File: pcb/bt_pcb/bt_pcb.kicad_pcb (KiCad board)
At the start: 4 copper layers, 130 x 65 mm, 224 parts, among them IC1 LTC3621EMS8E-25#PBF, IC2 ADAU1961WBCPZ-R7, IC3 STM32H750VBT6, IC4 STM32H523CEU6, IC5 W25Q512JVEIM, J1 Conn_01x02, J10 Conn_01x04, J11 Conn_01x04, J12 Conn_01x05, J13 FTSH-107-01-L-DV-K-A, J14 FTSH-107-01-L-DV-K-A, J15 Conn_01x08, J16 ReanNYS216G, J17 ReanNYS216G, J18 ReanNYS216G, J19 ReanNYS216G, J2 694106301002, J3 Conn_01x01, J4 Conn_01x01, J5 Conn_01x03, J6 UJ32-C-H-G-SMT-TR-68, J7 Conn_01x04, J8 Conn_01x10, J9 Conn_01x04, SW1 SW_Push, SW2 SW_Push, SW3 SW_Push, SW4 SW_Push, SW5 SW_Push, SW6 SW_Push, SW7 SW_Push, SW8 SW_Push, SW9 SW_Push, U1 TLV76133DCY, U2 TLV76133DCY, U3 MCP6004, U4 MCP6004

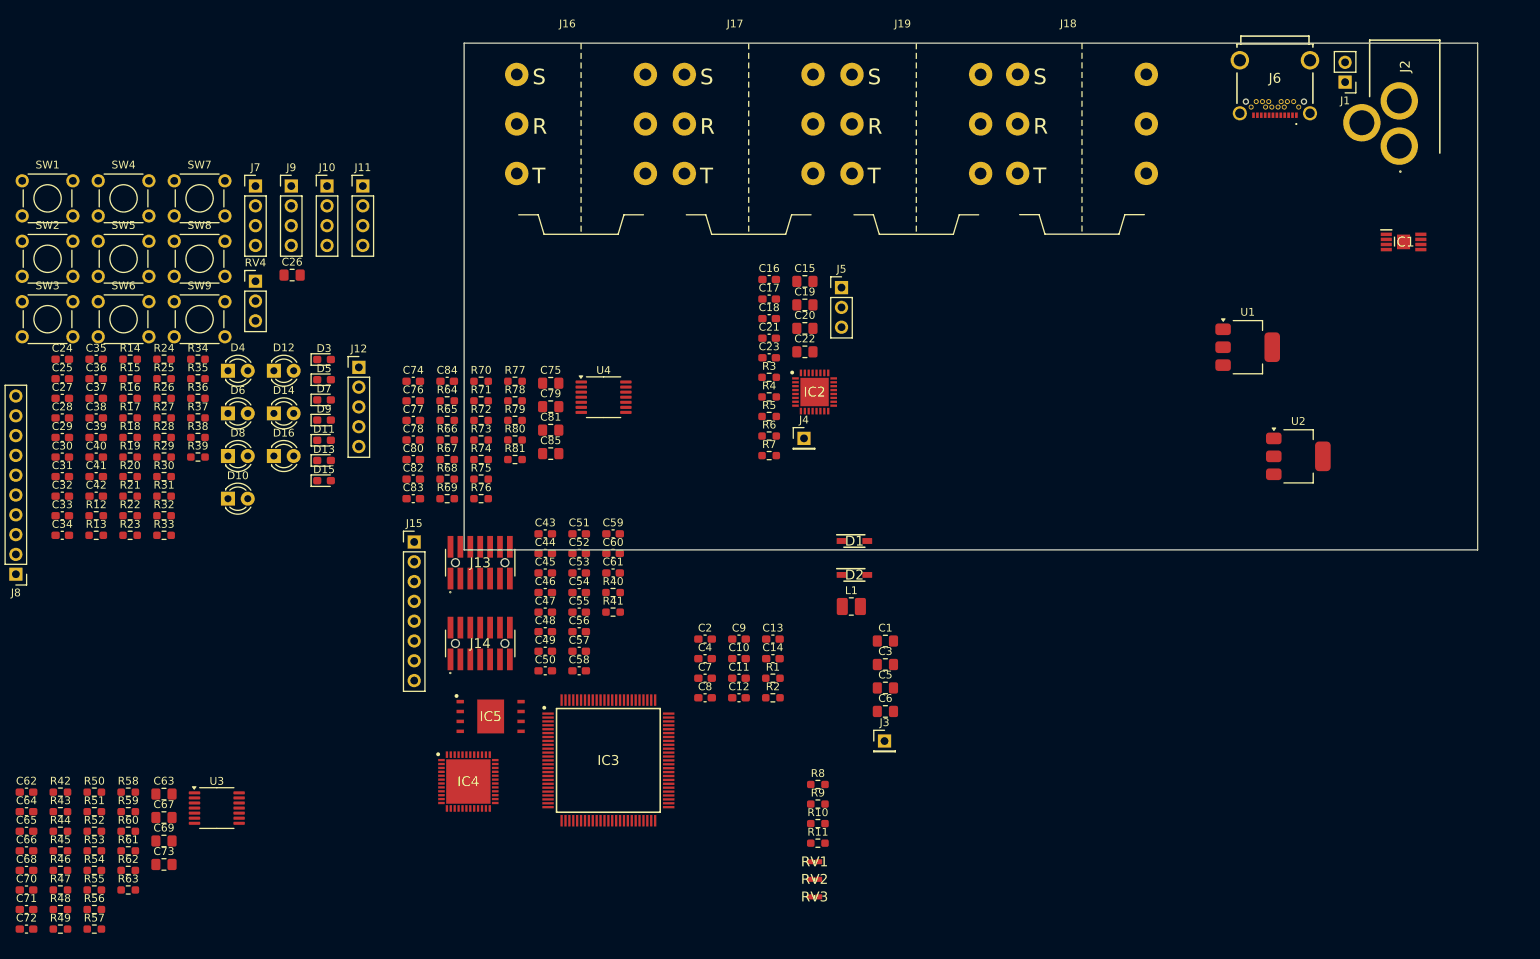
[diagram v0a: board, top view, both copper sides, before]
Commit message: pcb with some schematic tuning
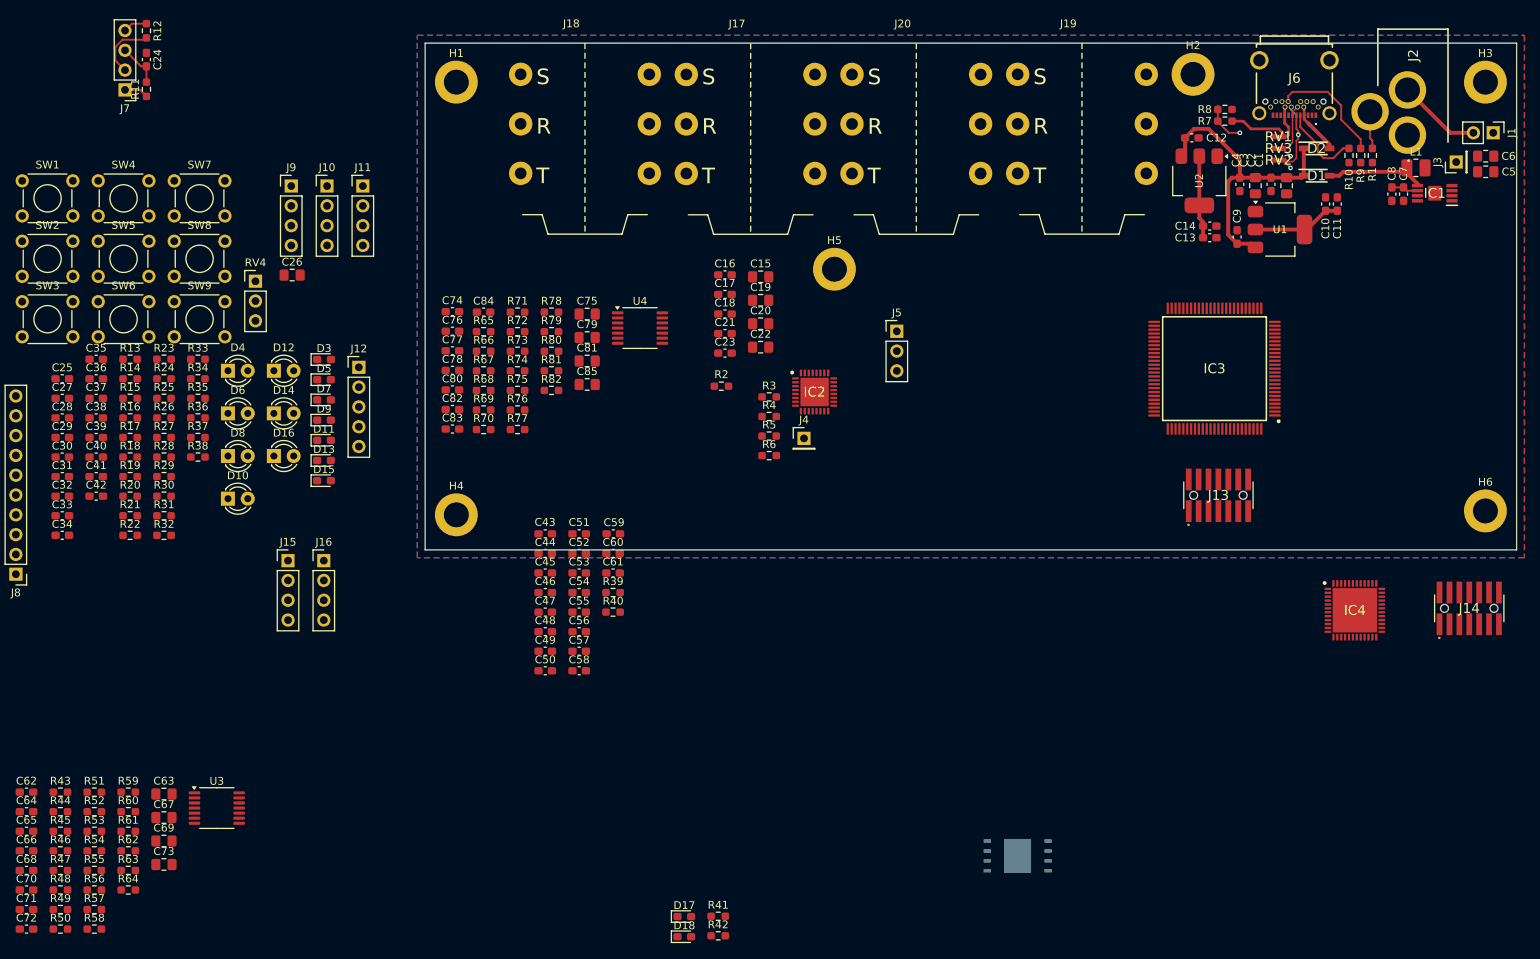
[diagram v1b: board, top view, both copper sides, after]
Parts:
- removed the R2 at (124.6, 151.5)
- added D17: LED, LED_SMD:LED_0603_1608Metric_Pad1.05x0.95mm_HandSolder, F.Cu at (113.2, 179.5)
- added D18: LED, LED_SMD:LED_0603_1608Metric_Pad1.05x0.95mm_HandSolder, F.Cu at (113.2, 182.1)
- added H1: MountingHole_Pad, MountingHole:MountingHole_3.2mm_M3_ISO14580_Pad, F.Cu at (84.0, 72.5)
- added H2: MountingHole_Pad, MountingHole:MountingHole_3.2mm_M3_ISO14580_Pad, F.Cu at (178.5, 71.5)
- added H3: MountingHole_Pad, MountingHole:MountingHole_3.2mm_M3_ISO14580_Pad, F.Cu at (216.0, 72.5)
- added H4: MountingHole_Pad, MountingHole:MountingHole_3.2mm_M3_ISO14580_Pad, F.Cu at (84.0, 128.0)
- added H5: MountingHole_Pad, MountingHole:MountingHole_3.2mm_M3_ISO14580_Pad, F.Cu at (132.5, 96.5)
- added H6: MountingHole_Pad, MountingHole:MountingHole_3.2mm_M3_ISO14580_Pad, F.Cu at (216.0, 127.5)
- added J16: Conn_01x04, Connector_PinHeader_2.54mm:PinHeader_1x04_P2.54mm_Vertical, F.Cu at (67.0, 133.9)
- added R41: 680, Resistor_SMD:R_0603_1608Metric_Pad0.98x0.95mm_HandSolder, F.Cu at (117.6, 179.5)
- added R42: 680, Resistor_SMD:R_0603_1608Metric_Pad0.98x0.95mm_HandSolder, F.Cu at (117.6, 182.0)
- IC5: moved to B.Cu
- J15: value Conn_01x08 -> Conn_01x04; footprint Connector_PinHeader_2.54mm:PinHeader_1x08_P2.54mm_Vertical -> Connector_PinHeader_2.54mm:PinHeader_1x04_P2.54mm_Vertical
- moved J14 126.9 mm to (213.9, 140.0)
- moved IC4 115.8 mm to (199.2, 140.2)
- moved RV3 112.9 mm to (189.4, 81.0)
- moved R10 111.5 mm to (198.5, 81.9), turned to -90 degrees
- moved R9 110.4 mm to (200.0, 81.9), turned to -90 degrees
- moved RV1 110.4 mm to (189.4, 79.5)
- moved RV2 109.8 mm to (189.4, 82.5)
- moved C8 109.2 mm to (204.0, 86.9), turned to -90 degrees
- moved C7 109.0 mm to (205.5, 86.9), turned to -90 degrees
- moved C6 104.9 mm to (216.0, 82.0)
- moved J3 104.4 mm to (212.2, 82.8), turned to 90 degrees
- moved R8 103.3 mm to (182.6, 76.0)
- moved R1 102.0 mm to (201.5, 81.9), turned to -90 degrees
- moved C5 101.6 mm to (216.0, 84.0)
- moved R7 99.8 mm to (182.6, 77.5), turned to 180 degrees
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- renumbered J16 to J17, J17 to J18, J18 to J19, J19 to J20, R11 to R10, R12 to R11, R13 to R12, R14 to R13, R15 to R14, R16 to R15, R17 to R16, R18 to R17, R19 to R18, R20 to R19, R3 to R2, R21 to R20, R22 to R21, R23 to R22, R24 to R23, R25 to R24, R26 to R25, R27 to R26, R28 to R27, R29 to R28, R30 to R29, R4 to R3, R31 to R30, R32 to R31, R33 to R32, R34 to R33, R35 to R34, R36 to R35, R37 to R36, R38 to R37, R39 to R38, R40 to R39, R5 to R4, R41 to R40, R42 to R43, R43 to R44, R44 to R45, R45 to R46, R46 to R47, R47 to R48, R48 to R49, R6 to R5, R49 to R50, R50 to R51, R51 to R52, R52 to R53, R53 to R54, R54 to R55, R55 to R56, R56 to R57, R57 to R58, R58 to R59, R7 to R6, R59 to R60, R60 to R61, R61 to R62, R62 to R63, R63 to R64, R64 to R65, R65 to R66, R66 to R67, R67 to R68, R68 to R69, R8 to R7, R69 to R70, R70 to R71, R71 to R72, R72 to R73, R73 to R74, R74 to R75, R75 to R76, R76 to R77, R77 to R78, R78 to R79, R9 to R8, R79 to R80, R80 to R81, R81 to R82, R10 to R9
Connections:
- C1 pad 1: Net-(D1-A) -> +5V
- C2 pad 1: Net-(D1-A) -> +5V
- C3 pad 1: Net-(D1-A) -> +5V
- C4 pad 1: Net-(D1-A) -> +5V
- C5 pad 1: Net-(IC1-VIN) -> Net-(IC1-RUN)
- C6 pad 1: Net-(IC1-VIN) -> Net-(IC1-RUN)
- IC1 pad 2: Net-(IC1-VIN) -> Net-(IC1-RUN)
- IC3 pad 65: GND -> AUX_1_TO_2
- IC3 pad 66: GND -> AUX_2_TO_1
- IC4 pad 10: GND -> AUX_2_TO_1
- IC4 pad 11: GND -> AUX_1_TO_2
- J1 pad 2: Net-(IC1-VIN) -> Net-(IC1-RUN)
- J15 pad 1: Net-(IC4-PB10) -> Net-(IC4-PA7)
- J15 pad 2: Net-(IC4-PB2) -> Net-(IC4-PA6)
- J15 pad 3: Net-(IC4-PB1) -> Net-(IC4-PA5)
- J15 pad 4: Net-(IC4-PB0) -> Net-(IC4-PA4)
- J2 pad 2: Net-(IC1-VIN) -> Net-(IC1-RUN)
- J6 pad A10: unconnected-(J6-SSRXN2-PadA10) -> GND
- J6 pad A11: unconnected-(J6-SSRXP2-PadA11) -> GND
- J6 pad A2: unconnected-(J6-SSTXP1-PadA2) -> GND
- J6 pad A3: unconnected-(J6-SSTXN1-PadA3) -> GND
- J6 pad A8: unconnected-(J6-SBU1-PadA8) -> GND
- J6 pad B10: unconnected-(J6-SSRXN1-PadB10) -> GND
- J6 pad B11: unconnected-(J6-SSRXP1-PadB11) -> GND
- J6 pad B2: unconnected-(J6-SSTXP2-PadB2) -> GND
- J6 pad B3: unconnected-(J6-SSTXN2-PadB3) -> GND
- J6 pad B8: unconnected-(J6-SBU2-PadB8) -> GND
- L1 pad 1: Net-(IC1-SW) -> Net-(D1-A)
- L1 pad 2: Net-(D1-A) -> Net-(IC1-SW)
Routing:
- net +5V: track 0.00 -> 38.6 mm
- net VBUS: track 0.00 -> 22.7 mm
- net Net-(J6-CC2): track 0.00 -> 15.0 mm
- net +3V3: track 0.00 -> 14.6 mm
- net USB_D-: track 0.00 -> 13.2 mm, vias 0 -> 2
- net Net-(D1-A): track 0.00 -> 12.3 mm
- net Net-(IC1-RUN): track 0.00 -> 10.7 mm
- net +3.3VA: track 0.00 -> 10.7 mm
- net Net-(J6-CC1): track 0.00 -> 10.5 mm
- net EXP_SW_0: track 0.00 -> 7.96 mm
- net USB_D+: track 0.00 -> 7.87 mm, vias 0 -> 1
- net EXP_0: track 0.00 -> 5.63 mm
- net VBUS_SENSE: track 0.00 -> 5.50 mm, vias 0 -> 1
- net Net-(J2-GND_2): track 0.00 -> 4.82 mm
- net Net-(IC1-INTVCC): track 0.00 -> 3.61 mm
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- added copper zone on B.Cu, net GND
- added copper zone on F.Cu, net GND
- added copper zone on In1.Cu, net GND
- added copper zone on In2.Cu, net GND
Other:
- board size 130 x 65 mm -> 140 x 65 mm

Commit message: idk
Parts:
- moved SW6 179.7 mm to (217.8, 100.2), turned to 180 degrees
- moved C39 176.8 mm to (212.9, 93.5)
- moved C40 175.9 mm to (212.9, 103.5)
- moved C41 175.3 mm to (212.8, 113.5)
- moved C42 175.1 mm to (212.9, 123.5)
- moved SW9 172.5 mm to (217.8, 130.2), turned to 180 degrees
- moved SW8 172.1 mm to (217.8, 120.2), turned to 180 degrees
- moved SW7 171.8 mm to (217.8, 110.2), turned to 180 degrees
- moved R35 166.5 mm to (216.2, 93.5)
- moved R36 165.7 mm to (216.2, 103.5)
- moved R38 165.4 mm to (216.2, 123.5)
- moved R37 165.4 mm to (216.1, 113.5)
- moved R26 162.3 mm to (208.2, 101.0)
- moved R27 161.9 mm to (208.2, 111.0)
- moved R29 161.9 mm to (208.2, 131.0)
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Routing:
- net +3V3: track 14.6 -> 65.0 mm
- net EXP_SW_0: track 7.96 -> 3.25 mm
- net Net-(IC1-RUN): track 10.7 -> 15.4 mm
- net EXP_2: track 0.00 -> 4.28 mm
- net EXP_1: track 0.00 -> 4.28 mm
- net EXP_3: track 0.00 -> 4.28 mm
- net GND: track 3.09 -> 0.00 mm
- net EXP_SW_3: track 0.00 -> 3.00 mm
- net EXP_SW_2: track 0.00 -> 3.00 mm
- net EXP_SW_1: track 0.00 -> 3.00 mm
- net Net-(D1-A): track 12.3 -> 9.96 mm
- net Net-(IC1-INTVCC): track 3.61 -> 1.64 mm
- net VBUS: track 22.7 -> 20.9 mm
- net USB_D+: track 7.87 -> 6.16 mm
- net +5V: track 38.6 -> 37.2 mm
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
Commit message: progress
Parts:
- C74, C75, C76, C77, C78, C79, C80, C81, C82, C83, C84, C85, R65, R66, R67, R68, R69, R70, R71, R72, R73, R74, R75, R76, U4: moved to B.Cu
- moved J14 272.2 mm to (-55.8, 103.8)
- moved IC4 221.5 mm to (-57.4, 121.5), turned to 0 degrees
- moved J13 216.1 mm to (-55.8, 93.4)
- moved IC5 176.1 mm to (-9.75, 93.8), turned to 0 degrees
- moved R41 174.4 mm to (-38.8, 102.3)
- moved R42 174.4 mm to (-38.8, 104.8)
- moved D17 166.8 mm to (-34.4, 102.0)
- moved D18 166.8 mm to (-34.4, 104.5)
- moved J5 161.8 mm to (-19.1, 131.3)
- moved J4 155.9 mm to (-23.9, 150.7)
- moved R3 155.9 mm to (-28.4, 145.3)
- moved R4 155.9 mm to (-28.4, 147.9)
- moved R5 155.9 mm to (-28.4, 150.4)
- moved R6 155.9 mm to (-28.4, 152.9)
- moved IC2 155.9 mm to (-22.5, 144.7)
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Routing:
- net +3V3: track 65.0 -> 105.0 mm
- net +5V: track 37.2 -> 0.00 mm
- net EXP_SW_0: track 3.25 -> 22.3 mm
- net EXP_0: track 4.38 -> 20.9 mm
- net Net-(IC1-RUN): track 15.4 -> 31.2 mm
- net EXP_SW_1: track 3.00 -> 16.4 mm
- net EXP_1: track 4.28 -> 15.9 mm
- net BTN_7_QB: track 0.00 -> 10.9 mm
- net BTN_6_QB: track 0.00 -> 10.9 mm
- net BTN_5_QB: track 0.00 -> 10.9 mm
- net BTN_8_QB: track 0.00 -> 10.9 mm
- net +3.3VA: track 10.7 -> 0.00 mm
- net Net-(IC1-PGOOD): track 0.00 -> 10.6 mm
- net EXP_SW_2: track 3.00 -> 10.3 mm
- net VBUS_SENSE: track 5.50 -> 0.00 mm, vias 1 -> 0
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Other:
- board size 140 x 65 mm -> 135 x 80.5 mm

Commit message: pcb now under revision
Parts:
- removed the C61 at (-38.8, 94.7)
- added C15: 10u, Capacitor_SMD:C_0805_2012Metric_Pad1.18x1.45mm_HandSolder, F.Cu at (117.8, 93.0)
- added C16: 1u, Capacitor_SMD:C_0603_1608Metric_Pad1.08x0.95mm_HandSolder, F.Cu at (119.5, 92.8)
- added C17: 100n, Capacitor_SMD:C_0603_1608Metric_Pad1.08x0.95mm_HandSolder, F.Cu at (121.0, 92.8)
- added C46: 100n, Capacitor_SMD:C_0603_1608Metric_Pad1.08x0.95mm_HandSolder, F.Cu at (92.2, 91.8)
- added C65: 2.2, Capacitor_SMD:C_0603_1608Metric_Pad1.08x0.95mm_HandSolder, B.Cu at (194.8, 100.2)
- added R39: 10k, Resistor_SMD:R_0603_1608Metric_Pad0.98x0.95mm_HandSolder, F.Cu at (93.8, 91.8)
- added SW10: SW_Push, Button_Switch_THT:SW_TH_Tactile_Omron_B3F-102x, F.Cu at (83.8, 89.8)
- C27: renamed from C24; moved to B.Cu
- C30: renamed from C27; moved to B.Cu
- C31: renamed from C28; moved to B.Cu
- C33: renamed from C30; moved to B.Cu
- C66: renamed from C62; moved to B.Cu
- C67: renamed from C63; moved to B.Cu
- C68: renamed from C64; moved to B.Cu
- C69: renamed from C65; moved to B.Cu
- C70: renamed from C66; moved to B.Cu
- C71: renamed from C67; moved to B.Cu
- C72: renamed from C68; moved to B.Cu
- C73: renamed from C69; moved to B.Cu
- C74: renamed from C70; moved to B.Cu
- C75: renamed from C71; moved to B.Cu
- C76: renamed from C72; moved to B.Cu
- C77: renamed from C73; moved to B.Cu
- J13, J14: value FTSH-107-01-L-DV-K-A -> Conn_01x05; footprint library:FTSH-107-XX-YYY-DV-K-A -> Connector_PinHeader_2.54mm:PinHeader_1x05_P2.54mm_Vertical
- R11, R12, R13, R14, R15, R16, R17, R19, R3, R4, R5, R6, U3: moved to B.Cu
- R44: renamed from R43; moved to B.Cu
- R45: renamed from R44; moved to B.Cu
- R46: renamed from R45; value 10k -> 470; moved to B.Cu
- R47: renamed from R46; moved to B.Cu
- R48: renamed from R47; moved to B.Cu
- R49: renamed from R48; moved to B.Cu
- R50: renamed from R49; moved to B.Cu
- R51: renamed from R50; value 10k -> 470; moved to B.Cu
- R52: renamed from R51; moved to B.Cu
- R53: renamed from R52; moved to B.Cu
- R54: renamed from R53; value 10k -> 470; moved to B.Cu
- R55: renamed from R54; moved to B.Cu
- R56: renamed from R55; moved to B.Cu
- R57: renamed from R56; moved to B.Cu
- R58: renamed from R57; moved to B.Cu
- R59: renamed from R58; value 10k -> 470; moved to B.Cu
- R60: renamed from R59; moved to B.Cu
- R61: renamed from R60; moved to B.Cu
- R62: renamed from R61; moved to B.Cu
- R63: renamed from R62; moved to B.Cu
- R64: renamed from R63; moved to B.Cu
- R65: renamed from R64; moved to B.Cu
- R78: renamed from R77; moved to B.Cu
- R79: renamed from R78; moved to B.Cu
- R80: renamed from R79; moved to B.Cu
- R81: renamed from R80; moved to B.Cu
- R82: renamed from R81; moved to B.Cu
- R83: renamed from R82; moved to B.Cu
- moved R23 304.3 mm to (211.8, 89.2), turned to 90 degrees
- moved R24 298.4 mm to (206.0, 89.3), turned to 90 degrees
- moved D4 298.3 mm to (214.3, 85.2), turned to 180 degrees
- moved D6 292.3 mm to (208.5, 85.2), turned to 180 degrees
- moved D3 284.7 mm to (212.8, 86.5), turned to 180 degrees
- moved D5 278.8 mm to (207.0, 86.5), turned to 180 degrees
- moved C32 261.8 mm to (156.1, 98.0)
- moved J8 257.3 mm to (145.3, 105.5), turned to -90 degrees
- moved R18 256.6 mm to (159.8, 98.0), turned to 180 degrees
- moved C28 252.0 mm to (144.2, 108.2), turned to 180 degrees
- moved J14 241.0 mm to (185.0, 112.8)
- moved C69 240.4 mm to (126.0, 79.2), turned to 90 degrees
- moved RV4 238.6 mm to (155.5, 95.5), turned to 90 degrees
- moved R49 237.6 mm to (125.2, 76.8), turned to 180 degrees
- moved C68 237.5 mm to (122.2, 73.0), turned to 90 degrees
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- renumbered C15 to C18, C16 to C19, C17 to C20, C18 to C21, C19 to C22, C20 to C23, C21 to C24, C22 to C25, C23 to C26, C25 to C28, C26 to C29, C29 to C32, C31 to C34, C32 to C35, C33 to C36, C34 to C37, C35 to C38, C36 to C39, C37 to C40, C38 to C41, C39 to C42, C40 to C43, C41 to C44, C42 to C45, C43 to C47, C44 to C48, C45 to C49, C46 to C50, C47 to C51, C48 to C52, C49 to C53, C50 to C54, C51 to C55, C52 to C56, C53 to C57, C54 to C58, C55 to C59, C56 to C60, C57 to C61, C58 to C62, C59 to C63, C60 to C64, C74 to C78, C75 to C79, C76 to C80, C77 to C81, C78 to C82, C79 to C83, C80 to C84, C81 to C85, C82 to C86, C83 to C87, C84 to C88, C85 to C89, R39 to R40, R40 to R41, R41 to R42, R42 to R43, R65 to R66, R66 to R67, R67 to R68, R68 to R69, R69 to R70, R70 to R71, R71 to R72, R72 to R73, R73 to R74, R74 to R75, R75 to R76, R76 to R77
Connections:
- IC3 pad 1: EXP_SW_0 -> INA_SW
- IC3 pad 2: EXP_SW_1 -> INB_SW
- IC3 pad 3: EXP_SW_2 -> OUTA_SW
- IC3 pad 4: EXP_SW_3 -> OUTB_SW
- IC3 pad 51: OUTB_SW -> EXP_SW_3
- IC3 pad 52: OUTA_SW -> EXP_SW_2
- IC3 pad 53: INB_SW -> EXP_SW_1
- IC3 pad 54: INA_SW -> EXP_SW_0
- IC4 pad 43: GND -> BTN_9_J
- J13 pad 1: unconnected-(J13-Pad1) -> GND
- J13 pad 2: unconnected-(J13-Pad2) -> MCU2_NRST
- J13 pad 3: +3V3 -> MCU2_DEB_SWCLK
- J13 pad 4: MCU1_DEB_SWDIO -> MCU2_DEB_SWDIO
- J13 pad 5: GND -> +3V3
- J14 pad 1: unconnected-(J14-Pad1) -> GND
- J14 pad 2: unconnected-(J14-Pad2) -> MCU1_NRST
- J14 pad 3: +3V3 -> MCU1_DEB_SWCLK
- J14 pad 4: MCU2_DEB_SWDIO -> MCU1_DEB_SWDIO
- J14 pad 5: GND -> +3V3
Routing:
- net VCOM: track 0.00 -> 115.4 mm, vias 0 -> 1
- net OUTB_SW: track 0.00 -> 111.7 mm, vias 0 -> 1
- net +3V3: track 105.0 -> 196.6 mm, vias 0 -> 20
- net OUTA_SW: track 0.00 -> 91.0 mm, vias 0 -> 1
- net BTN_9_J: track 0.00 -> 82.1 mm
- net USB_D-: track 8.01 -> 82.5 mm, vias 2 -> 3
- net USB_D+: track 8.56 -> 80.0 mm, vias 1 -> 2
- net INB_SW: track 0.00 -> 70.3 mm, vias 0 -> 1
- net LED_0_RD: track 0.00 -> 68.7 mm
- net BTN_5_QB: track 10.9 -> 77.9 mm
- net VBUS_SENSE: track 0.00 -> 66.5 mm, vias 0 -> 2
- net EXP_SW_3: track 6.42 -> 72.6 mm, vias 0 -> 1
- net LED_2_QB: track 0.00 -> 65.1 mm
- net BTN_6_QB: track 10.9 -> 70.6 mm
- net LED_3_QB: track 0.00 -> 57.7 mm
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- added copper zone on In1.Cu, net +3.3VA
- added copper zone on In1.Cu, net +3V3
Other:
- board text added: "busy-toad rev. A"

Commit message: continuing review
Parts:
- moved R39 9.55 mm to (87.2, 98.8), turned to 180 degrees
- moved C46 7.43 mm to (87.2, 97.2), turned to 0 degrees
- moved SW10 5.59 mm to (89.2, 88.8), turned to -90 degrees
- moved SW2 5.59 mm to (84.8, 115.2), turned to 90 degrees
- moved J13 5.54 mm to (115.5, 114.2), turned to 180 degrees
- moved C40 4.00 mm to (108.0, 116.2)
- moved R33 4.00 mm to (108.0, 117.8)
- moved SW4 4.00 mm to (103.8, 109.8)
- moved C39 3.13 mm to (90.2, 117.8)
- moved R32 3.13 mm to (90.2, 119.2)
- moved C37 2.83 mm to (102.2, 102.0)
- moved R30 2.83 mm to (103.8, 102.0)
- moved SW1 2.83 mm to (93.8, 99.8)
- moved SW5 2.83 mm to (93.8, 119.8)
- moved C41 2.09 mm to (104.6, 121.8)
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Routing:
- net GND: track 56.5 -> 70.3 mm, vias 4 -> 6
- net BTN_9_J: track 82.1 -> 71.6 mm
- net MCU2_DEB_SWDIO: track 7.98 -> 14.1 mm
- net +3V3: track 196.6 -> 192.2 mm
- net BTN_3_J: track 29.5 -> 25.5 mm
- net BTN_0_J: track 38.3 -> 35.5 mm
- net BTN_4_J: track 30.6 -> 28.1 mm
- net BTN_1_J: track 56.4 -> 53.9 mm
- net Net-(U4D-+): track 13.9 -> 15.9 mm
- net Net-(U4B-+): track 15.5 -> 17.5 mm
- net Net-(C68-Pad2): track 16.7 -> 18.3 mm
- net Net-(C67-Pad1): track 7.58 -> 9.21 mm
- net MCU2_DEB_SWCLK: track 7.92 -> 9.52 mm
- net MCU2_NRST: track 27.9 -> 27.1 mm, vias 2 -> 1
- net LED_5_QB: track 50.6 -> 49.8 mm
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
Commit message: first notes
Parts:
- removed the C37 at (102.2, 102.0)
- removed the C38 at (87.2, 106.8)
- removed the C39 at (90.2, 117.8)
- removed the C40 at (108.0, 116.2)
- removed the C41 at (104.6, 121.8)
- removed the C42 at (207.5, 99.7)
- removed the C43 at (207.5, 109.7)
- removed the C44 at (207.5, 119.7)
- removed the C45 at (207.5, 129.7)
- removed the C46 at (87.2, 97.2)
- added R39: 10k, Resistor_SMD:R_0603_1608Metric_Pad0.98x0.95mm_HandSolder, F.Cu at (179.0, 110.2)
- added R40: 10k, Resistor_SMD:R_0603_1608Metric_Pad0.98x0.95mm_HandSolder, F.Cu at (112.5, 121.5)
- J6: value UJ32-C-H-G-SMT-TR-68 -> USB_C_Receptacle_USB2.0_16P; footprint library:UJ32CHGSMTTR68 -> Connector_USB:USB_C_Receptacle_GCT_USB4105-xx-A_16P_TopMnt_Horizontal
- moved R8 17.4 mm to (197.0, 72.0), turned to 0 degrees
- moved R7 16.8 mm to (197.0, 70.2), turned to 180 degrees
- moved R31 14.1 mm to (104.2, 117.8), turned to 0 degrees
- moved RV1 9.80 mm to (197.2, 68.5), turned to 0 degrees
- moved R9 7.95 mm to (200.0, 69.0)
- moved RV3 4.38 mm to (203.8, 68.8), turned to 90 degrees
- moved RV2 4.14 mm to (201.5, 68.8), turned to 90 degrees
- moved R10 4.10 mm to (206.2, 69.0)
- moved R33 1.87 mm to (103.5, 121.8), turned to -90 degrees
- moved R29 1.77 mm to (102.5, 100.8)
- moved J6 1.75 mm to (202.0, 62.2)
- moved R30 1.60 mm to (88.2, 106.5)
- moved R38 1.60 mm to (88.2, 97.5)
- renumbered C47 to C37, C48 to C38, C49 to C39, C50 to C40, C51 to C41, C52 to C42, C53 to C43, C54 to C44, C55 to C45, C56 to C46, C57 to C47, C58 to C48, C59 to C49, C60 to C50, C61 to C51, C62 to C52, C63 to C53, C64 to C54, C65 to C55, C66 to C56, C67 to C57, C68 to C58, C69 to C59, C70 to C60, C71 to C61, C72 to C62, C73 to C63, C74 to C64, C75 to C65, C76 to C66, C77 to C67, C78 to C68, C79 to C69, C80 to C70, C81 to C71, C82 to C72, C83 to C73, C84 to C74, C85 to C75, C86 to C76, C87 to C77, C88 to C78, C89 to C79, R9 to R10, R19 to R18, R20 to R19, R21 to R20, R22 to R21, R23 to R22, R24 to R23, R25 to R24, R26 to R25, R27 to R26, R28 to R27, R29 to R28, R30 to R29, R31 to R30, R32 to R31, R33 to R32, R34 to R33, R35 to R34, R36 to R35, R37 to R36, R38 to R37, R39 to R38, R40 to R41, R41 to R42, R42 to R43, R43 to R44, R44 to R45, R45 to R46, R46 to R47, R47 to R48, R48 to R49, R49 to R50, R50 to R51, R51 to R52, R52 to R53, R53 to R54, R54 to R55, R55 to R56, R56 to R57, R57 to R58, R58 to R59, R59 to R60, R60 to R61, R61 to R62, R62 to R63, R63 to R64, R64 to R65, R65 to R66, R66 to R67, R67 to R68, R68 to R69, R69 to R70, R70 to R71, R71 to R72, R72 to R73, R73 to R74, R74 to R75, R75 to R76, R76 to R77, R77 to R78, R78 to R79, R79 to R80, R80 to R81, R81 to R82, R82 to R83, R83 to R84, R10 to R9
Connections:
- IC3 pad 94: GND -> Net-(IC3-BOOT0)
- IC4 pad 44: GND -> Net-(IC4-BOOT0)
- J13 pad 1: GND -> MCU2_NRST
- J13 pad 2: MCU2_NRST -> MCU2_DEB_SWDIO
- J13 pad 3: MCU2_DEB_SWCLK -> GND
- J13 pad 4: MCU2_DEB_SWDIO -> MCU2_DEB_SWCLK
- J14 pad 1: GND -> MCU1_NRST
- J14 pad 2: MCU1_NRST -> MCU1_DEB_SWDIO
- J14 pad 3: MCU1_DEB_SWCLK -> GND
- J14 pad 4: MCU1_DEB_SWDIO -> MCU1_DEB_SWCLK
- R10 pad 1: Net-(J6-CC2) -> Net-(J6-CC1)
- R9 pad 1: Net-(J6-CC1) -> Net-(J6-CC2)
- RV4 pad 3: Net-(R18-Pad1) -> GND
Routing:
- net +3V3: track 192.2 -> 144.7 mm
- net VBUS: track 25.9 -> 14.9 mm, vias 1 -> 0
- net Net-(J6-CC2): track 11.7 -> 2.26 mm
- net MCU1_DEB_SWCLK: track 13.0 -> 21.6 mm
- net MCU1_DEB_SWDIO: track 13.1 -> 21.5 mm
- net USB_D-: track 82.5 -> 75.2 mm, vias 3 -> 2
- net Net-(IC4-BOOT0): track 0.00 -> 5.52 mm
- net VBUS_SENSE: track 66.5 -> 71.9 mm
- net BTN_2_J: track 55.6 -> 50.6 mm
- net USB_D+: track 80.0 -> 75.3 mm
- net MCU2_DEB_SWCLK: track 9.52 -> 14.1 mm
- net MCU2_NRST: track 27.1 -> 23.3 mm
- net BTN_1_J: track 53.9 -> 50.4 mm
- net BTN_9_J: track 71.6 -> 68.3 mm
- net MCU1_NRST: track 36.6 -> 33.2 mm
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- added copper zone on F.Cu, net VBUS
